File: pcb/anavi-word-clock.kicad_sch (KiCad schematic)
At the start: 10 parts, among them J3 Conn_01x04_Female, J7 Screw_Terminal_01x03, SW1 SW_DIP_x01, U1 MOUDLE-SEEEDUINO-XIAO-ESP32C3, U2 74LVC1G17W5-7

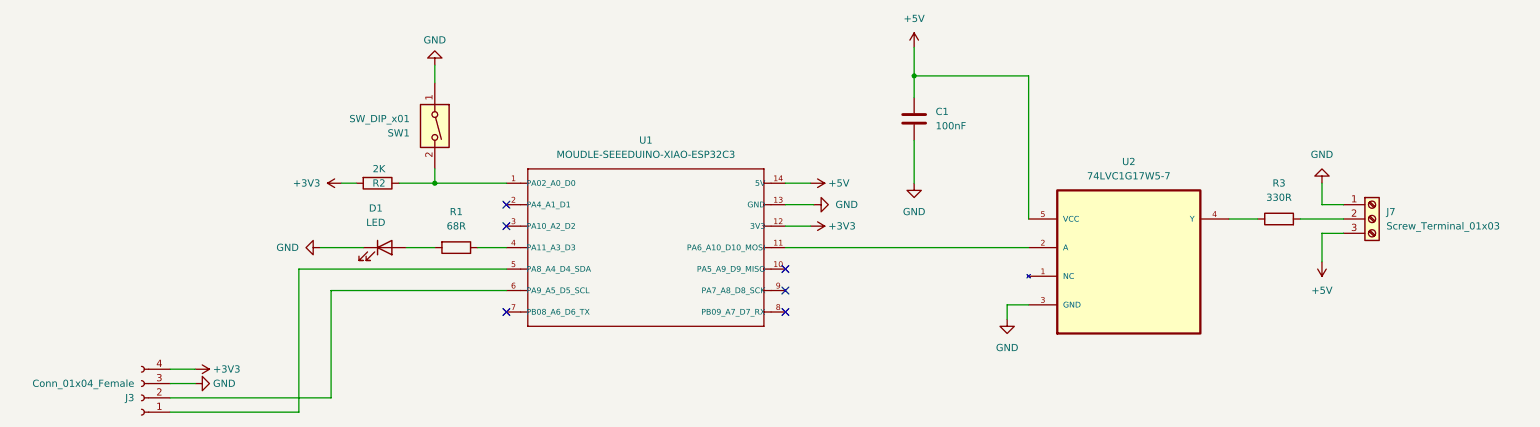
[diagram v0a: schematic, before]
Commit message: pcb: Change the PCB design
Update the schematics and change the PCB design to support I2C RTC
module with 1x6 female connector.

Signed-off-by: Leon Anavi <leon@anavi.org>
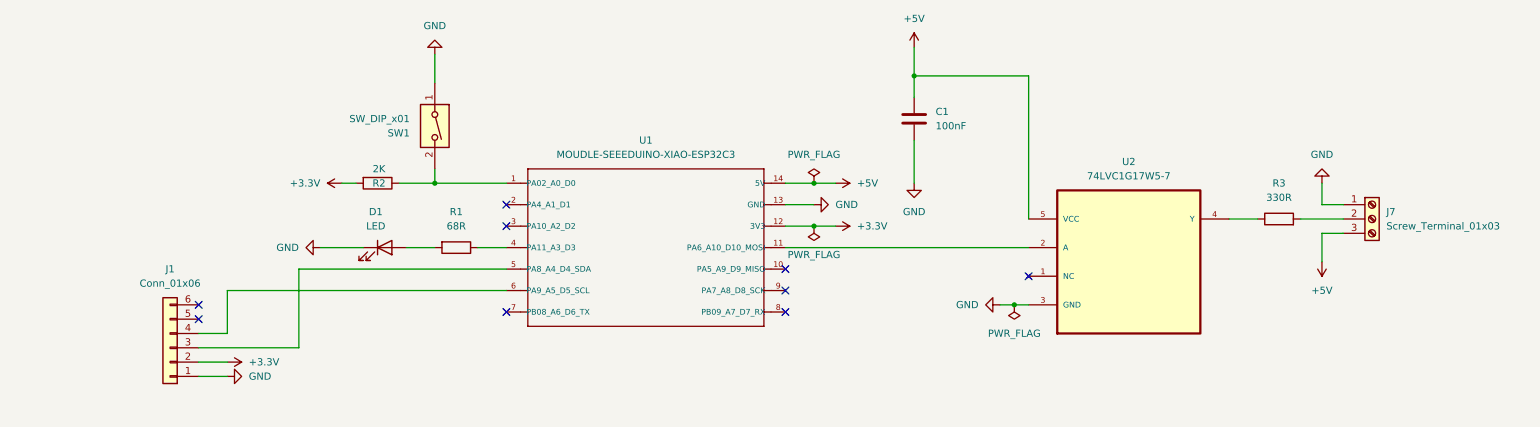
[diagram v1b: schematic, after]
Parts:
- removed J3: Conn_01x04_Female, Connector_PinHeader_2.54mm:PinHeader_1x04_P2.54mm_Vertical, symbol Connector:Conn_01x04_Female
- added J1: Conn_01x06, Connector_PinSocket_2.54mm:PinSocket_1x06_P2.54mm_Horizontal, symbol Connector_Generic:Conn_01x06
- SW1: footprint Button_Switch_THT:SW_PUSH_6mm_H4.3mm -> TL1105SF160Q:SW_TL1105SF160Q_EWI
- U2: footprint SOT95P280X145-5N -> SOT95P280X145-5N:SOT95P280X145-5N
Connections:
- net GND: now also J1.1 (Pin_1)
- net at U1.5 (PA8_A4_D4_SDA): now also J1.3 (Pin_3)
- net at U1.6 (PA9_A5_D5_SCL): now also J1.4 (Pin_4)
- net +3V3 renamed +3.3V
- net +3.3V: now also J1.2 (Pin_2)
- no-connect marks 6 -> 9

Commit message: pcb: Use XIAO ESP32C6
Switch the footprint from XIAO ESP32C3 to ESP32C6 because of the
on-board antenna with up to 80m BLE/Wi-Fi range which makes the
assembly of the clock easier.

Signed-off-by: Leon Anavi <leon@anavi.org>
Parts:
- U1: value MOUDLE-SEEEDUINO-XIAO-ESP32C3 -> XIAO ESP32C6; footprint xiao ESP32C3_PCB:MOUDLE14P-SMD-2.54-21X17.8MM -> xiao-esp32c6:XIAO-ESP32-C6-SMD
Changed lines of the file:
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@@
 			)
 		)
-		(property "Value" "MOUDLE-SEEEDUINO-XIAO-ESP32C3"
+		(property "Value" "XIAO ESP32C6"
 			(at 126.365 59.69 0)
 			(show_name no)
@@
 			)
 		)
-		(property "Footprint" "xiao ESP32C3_PCB:MOUDLE14P-SMD-2.54-21X17.8MM"
+		(property "Footprint" "xiao-esp32c6:XIAO-ESP32-C6-SMD"
 			(at 127 76.2 0)
 			(hide yes)

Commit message: anavi-word-clock.kicad_sch: Adjust schematics
Adjust schematics and remove capacitor from the PCB.

Signed-off-by: Leon Anavi <leon@anavi.org>
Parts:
- removed C1: 100nF, symbol Device:C
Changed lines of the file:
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@@
-	)
-	(junction
-		(at 173.99 45.72)
-		(diameter 0)
-		(color 0 0 0 0)
 	)
 	(junction
@@
 	(wire
 		(pts
-			(xy 173.99 57.15) (xy 173.99 64.77)
-		)
-		(stroke
-			(width 0)
-			(type default)
-		)
-	)
-	(wire
-		(pts
 			(xy 189.23 86.36) (xy 191.77 86.36)
 		)
@@
 	(wire
 		(pts
-			(xy 173.99 40.64) (xy 173.99 45.72)
-		)
-		(stroke
-			(width 0)
-			(type default)
-		)
-	)
-	(wire
-		(pts
 			(xy 46.99 93.98) (xy 64.77 93.98)
 		)
@@
 	(wire
 		(pts
-			(xy 173.99 45.72) (xy 173.99 49.53)
-		)
-		(stroke
-			(width 0)
-			(type default)
-		)
-	)
-	(wire
-		(pts
 			(xy 101.6 80.01) (xy 64.77 80.01)
 		)
@@
 		(pts
 			(xy 52.07 83.82) (xy 52.07 91.44)
-		)
-		(stroke
-			(width 0)
-			(type default)
-		)
-	)
-	(wire
-		(pts
-			(xy 173.99 45.72) (xy 194.31 45.72)
 		)
 		(stroke
@@
 	(symbol
 		(lib_id "power:+5V")
-		(at 173.99 40.64 0)
+		(at 194.31 45.72 0)
 		(unit 1)
 		(body_style 1)
@@
 		(fields_autoplaced yes)
 		(property "Reference" "#PWR04"
-			(at 173.99 44.45 0)
+			(at 194.31 49.53 0)
 			(hide yes)
 			(show_name no)
@@
 		)
 		(property "Value" "+5V"
-			(at 173.99 35.56 0)
+			(at 194.31 40.64 0)
 			(show_name no)
 			(do_not_autoplace no)
@@
 		)
 		(property "Footprint" ""
-			(at 173.99 40.64 0)
+			(at 194.31 45.72 0)
 			(hide yes)
 			(show_name no)
@@
 		)
 		(property "Datasheet" ""
-			(at 173.99 40.64 0)
+			(at 194.31 45.72 0)
 			(hide yes)
 			(show_name no)
@@
 		)
 		(property "Description" "Power symbol creates a global label with name \"+5V\""
-			(at 173.99 40.64 0)
+			(at 194.31 45.72 0)
 			(hide yes)
 			(show_name no)
@@
 	)
 	(symbol
-		(lib_name "GND_2")
-		(lib_id "power:GND")
-		(at 173.99 64.77 0)
-		(unit 1)
-		(body_style 1)
-		(exclude_from_sim no)
-		(in_bom yes)
-		(on_board yes)
-		(in_pos_files yes)
-		(dnp no)
-		(fields_autoplaced yes)
-		(property "Reference" "#PWR08"
-			(at 173.99 71.12 0)
-			(hide yes)
-			(show_name no)
-			(do_not_autoplace no)
-			(effects
-				(font
-					(size 1.27 1.27)
-				)
-			)
-		)
-		(property "Value" "GND"
-			(at 173.99 69.85 0)
-			(show_name no)
-			(do_not_autoplace no)
-			(effects
-				(font
-					(size 1.27 1.27)
-				)
-			)
-		)
-		(property "Footprint" ""
-			(at 173.99 64.77 0)
-			(hide yes)
-			(show_name no)
-			(do_not_autoplace no)
-			(effects
-				(font
-					(size 1.27 1.27)
-				)
-			)
-		)
-		(property "Datasheet" ""
-			(at 173.99 64.77 0)
-			(hide yes)
-			(show_name no)
-			(do_not_autoplace no)
-			(effects
-				(font
-					(size 1.27 1.27)
-				)
-			)
-		)
-		(property "Description" "Power symbol creates a global label with name \"GND\" , ground"
-			(at 173.99 64.77 0)
-			(hide yes)
-			(show_name no)
-			(do_not_autoplace no)
-			(effects
-				(font
-					(size 1.27 1.27)
-				)
-			)
-		)
-		(pin "1"
-		)
-		(instances
-			(project "anavi-word-clock"
-				(path "/2ff006f4-2a61-440d-9643-0ab2f7506f70"
-					(reference "#PWR08")
-					(unit 1)
-				)
-			)
-		)
-	)
-	(symbol
 		(lib_id "power:+3.3V")
 		(at 72.39 64.77 90)
@@
 					(unit 1)
 				)
-			)
-		)
-	)
-	(symbol
-		(lib_id "Device:C")
-		(at 173.99 53.34 0)
-		(unit 1)
-		(body_style 1)
-		(exclude_from_sim no)
-		(in_bom yes)
-		(on_board yes)
-		(in_pos_files yes)
-		(dnp no)
-		(fields_autoplaced yes)
-		(property "Reference" "C1"
-			(at 177.8 52.0699 0)
-			(show_name no)
-			(do_not_autoplace no)
-			(effects
-				(font
-					(size 1.27 1.27)
-				)
-				(justify left)
-			)
-		)
-		(property "Value" "100nF"
-			(at 177.8 54.6099 0)
-			(show_name no)
-			(do_not_autoplace no)
-			(effects
-				(font
-					(size 1.27 1.27)
-				)
-				(justify left)
-			)
-		)
-		(property "Footprint" ""
-			(at 174.9552 57.15 0)
-			(hide yes)
-			(show_name no)
-			(do_not_autoplace no)
-			(effects
-				(font
-					(size 1.27 1.27)
-				)
-			)
-		)
-		(property "Datasheet" ""
-			(at 173.99 53.34 0)
-			(hide yes)
-			(show_name no)
-			(do_not_autoplace no)
-			(effects
-				(font
-					(size 1.27 1.27)
-				)
-			)
-		)
-		(property "Description" ""
-			(at 173.99 53.34 0)
-			(hide yes)
-			(show_name no)
-			(do_not_autoplace no)
-			(effects
-				(font
-					(size 1.27 1.27)
-				)
-			)
-		)
-		(pin "1"
-		)
-		(pin "2"
-		)
-		(instances
-			(project "anavi-word-clock"
-				(path "/2ff006f4-2a61-440d-9643-0ab2f7506f70"
-					(reference "C1")
-					(unit 1)
-				)
